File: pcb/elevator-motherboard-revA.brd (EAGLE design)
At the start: 160 x 100 mm, 55 parts, among them J3 MAGJACK, J4 MAGJACK, J5 MAGJACK, J6 POWER_JACK, J8 MAGJACK, Q1 NCV8403BDTRKG, Q2 MOSFET_NCH_DUAL-SO08, Q3 MOSFET_NCH_DUAL-SO08, Q4 MOSFET_NCH_DUAL-SO08, Q5 NCV8403BDTRKG, Q6 MOSFET_NCH_DUAL-SO08, Q7 NCV8403BDTRKG, Q8 NCV8403BDTRKG, Q9 NCV8403BDTRKG, U2 TPD2E001, U3 TPD2E001, U4 74HC2G125, U5 TPD2E001, U7 TPD2E001

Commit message: motherboard schematic is done
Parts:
- removed C19: 0.1uF, microbuilder:0603
- removed PP3, PP4: MC2, con-phoenix-381_l:MC2
- added J1, J10, J7: (no value), SparkFun-Connectors:1X03
- added J9: (no value), SparkFun-Connectors:1X06_NO_SILK
- added LED1, LED2, LED3, LED4: LED-GREEN0603, BeagleBone_Blue_R3:0603-GREEN
- added OUT2: MC4, con-phoenix-381_l:MC4
- added R10, R13, R14, R7, R8, R9: (no value), adafruit:R0603
- added X1, X2, X3, X4: MSTBA2, con-phoenix-508:MSTBA2
- renumbered OUT4 to OUT1
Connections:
- new net B2B_RX1: J9.5, U$1.0/RX
- new net B2B_RX2: J9.6, U$1.2
- new net B2B_TX1: J9.3, U$1.1/TX
- new net B2B_TX2: J9.4, U$1.3/CANTX
- new net BOARD_ID: J10.2, U$1.15/A1
- new net IO1: J2.1, U$1.4/CANRX
- new net IO2: J2.2, U$1.5
- new net IO3: J2.3, U$1.6
- new net IO4: J2.4, U$1.7
- new net IO5: J2.5, U$1.12/MISO
- new net IO6: J2.6, U$1.24
- new net IO7: J2.7, U$1.25
- new net IO8: J2.8, U$1.26
- new net IO9: J2.9, U$1.27
- new net N$23: LED1.A, R9.1
- new net N$24: LED2.A, R10.1
- new net N$25: LED3.A, R7.1
- new net N$26: LED4.A, R8.1
- new net N$27: J10.3, R13.1
- new net N$33: J10.1, R14.2
- new net N$50: U$1.23/A9
- new net N$51: U$1.22/A8
- new net N$60: U$1.13/SCK
- new net N$61: U$1.GND2
- net 12V: now also J1.1, J2.10, J7.1, J7.2, OUT1.1, R8.2, X3.1; no longer OUT1.4
- net 24V: now also J1.2, J1.3, J7.3, OUT1.4, OUT2.4, R10.2, X1.1, X2.1; no longer PP3.1, PP4.1
- net 5V: now also OUT2.1, R7.2, U$1.VIN, X4.1; no longer OUT1.1
- net A.M1: now also U$1.30
- net A.M2: now also U$1.31/A12
- net A.SW1: now also U$1.28
- net A.SW2: now also U$1.29
- net B.M1: now also U$1.34/A15
- net B.M2: now also U$1.33/A14
- net B.SW1: now also U$1.32/A13
- net B.SW2: now also U$1.35/A16
- net C.M1: now also U$1.37/A18
- net C.M2: now also U$1.36/A17
- net C.SW1: now also U$1.39/A20
- net C.SW2: now also U$1.38/A19
- net D.M1: now also U$1.19/A5/SCL
- net D.M2: now also U$1.18/A4/SDA
- net D.SW1: now also U$1.9/CS
- net D.SW2: now also U$1.11/MOSI
- net GND: now also J2.12, J9.2, LED1.C, LED2.C, LED3.C, LED4.C, OUT2.2, OUT2.3, R14.1, X1.2, X2.2, X3.2, X4.2; no longer PP3.2, PP4.2
- net LEDS1: now also U$1.8
- net LEDS2: now also U$1.10/CS
- net PWM1: now also U$1.14/A0
- net PWM2: now also U$1.16/A2
- net PWM3: now also U$1.17/A3
- net PWM4: now also U$1.20/A6
- net PWM5: now also U$1.21/A7
- net VCC: now also J2.11, J9.1, R13.2, R9.2

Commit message: backup
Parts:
- moved X3 191.7 mm to (146.0, 88.0), turned to 90 degrees
- moved J7 174.8 mm to (130.0, 91.0), turned to 90 degrees
- moved R13 170.2 mm to (9.00, 82.0)
- moved R14 168.2 mm to (9.00, 76.0)
- moved J10 160.0 mm to (4.00, 77.0), turned to 90 degrees
- moved J1 159.1 mm to (112.0, 91.0), turned to 90 degrees
- moved X4 157.1 mm to (10.0, 98.0), turned to 180 degrees
- moved LED1 153.9 mm to (88.0, 59.0)
- moved LED2 153.9 mm to (91.0, 59.0)
- moved LED3 153.9 mm to (94.0, 59.0)
- moved LED4 153.9 mm to (88.0, 53.0)
- moved R10 153.9 mm to (92.0, 54.0)
- moved R7 153.9 mm to (88.0, 48.0)
- moved R8 153.9 mm to (91.0, 48.0)
- moved R9 153.9 mm to (94.0, 48.0)
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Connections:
- new net N$34: J7.2, PP1.1
- net 12V: no longer J7.2, PP1.1
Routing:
- net 24V: track 0.00 -> 241.0 mm
- net PWM1: track 0.00 -> 92.8 mm
- net PWM2: track 0.00 -> 84.8 mm
- net PWM3: track 0.00 -> 79.3 mm
- net PWM4: track 0.00 -> 77.5 mm
- net PWM5: track 0.00 -> 70.0 mm
- net 12V: track 0.00 -> 62.8 mm
- added copper zone on layer 1, net GND
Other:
- board size 160 x 100 mm -> 148 x 100 mm

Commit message: wip
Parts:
- moved C10 8.68 mm to (55.9, 88.2), turned to 180 degrees
- moved C1 7.54 mm to (72.5, 88.3), turned to 180 degrees
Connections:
- new net N$35: J1.2, PP2.1
- net 24V: no longer J1.2, PP2.1
- net GND: now also Q5.3, Q7.3, Q8.3, Q9.3
- net N$5: now also PL2.2; no longer PL1.2
- net N$6: now also PL1.2; no longer PL2.2
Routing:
- net 5V: track 0.00 -> 90.9 mm
- net LEDS1: track 0.00 -> 49.7 mm, vias 0 -> 1
- net LEDS2: track 0.00 -> 47.3 mm, vias 0 -> 1
- net N$5: track 0.00 -> 18.2 mm
- net N$6: track 0.00 -> 17.6 mm
- net N$16: track 0.00 -> 17.2 mm
- net N$13: track 0.00 -> 15.8 mm
- net N$15: track 0.00 -> 15.1 mm
- net N$14: track 0.00 -> 13.7 mm
- net N$4: track 0.00 -> 13.3 mm
- net N$35: track 0.00 -> 6.84 mm
- net N$34: track 0.00 -> 6.65 mm
- net 12V: track 62.8 -> 60.2 mm

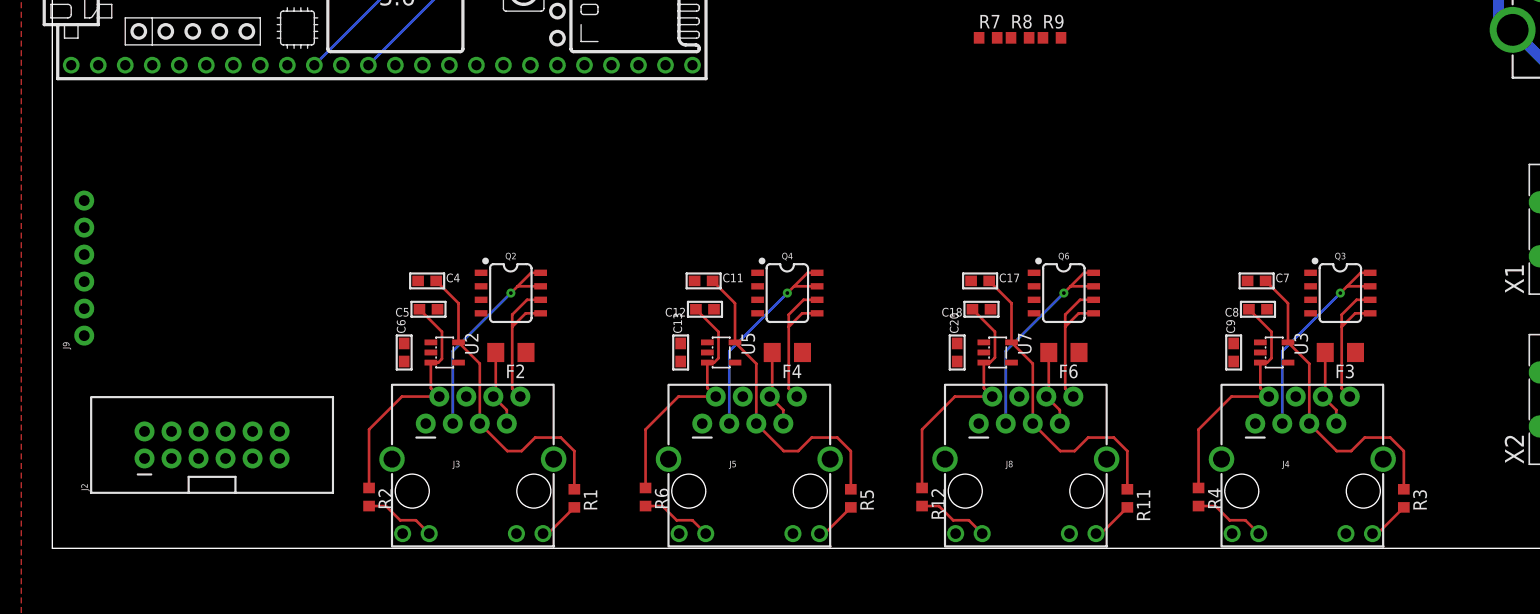
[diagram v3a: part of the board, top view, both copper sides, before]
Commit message: better placement
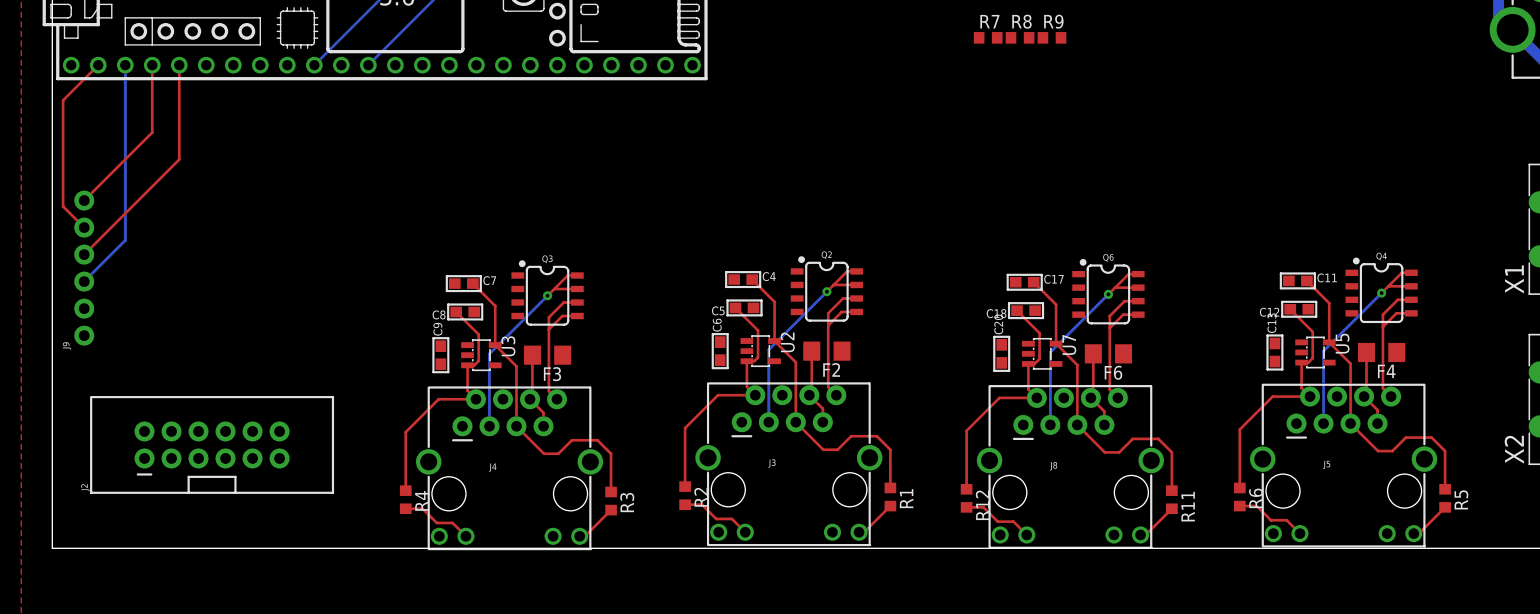
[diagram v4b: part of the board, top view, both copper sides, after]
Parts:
- moved C7 74.5 mm to (38.7, 24.9)
- moved R3 74.5 mm to (52.5, 4.45)
- moved R4 74.5 mm to (33.2, 4.57)
- moved U3 74.5 mm to (40.3, 18.2)
- moved C8 74.5 mm to (38.8, 22.2)
- moved C9 74.5 mm to (36.5, 18.2)
- moved F3 74.5 mm to (46.6, 18.2)
- moved J4 74.5 mm to (35.4, -5.97)
- moved Q3 74.5 mm to (46.6, 23.7)
- moved F4 55.9 mm to (125.0, 18.4)
- moved Q4 55.9 mm to (125.0, 24.0)
- moved R5 55.9 mm to (131.0, 4.70)
- moved C12 55.9 mm to (117.3, 22.5)
- moved C13 55.9 mm to (115.0, 18.4)
- moved J5 55.9 mm to (113.8, -5.71)
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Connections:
- net B.SW1: now also U$1.36/A17; no longer U$1.32/A13
- net C.M1: now also U$1.38/A19; no longer U$1.37/A18
- net C.M2: now also U$1.37/A18; no longer U$1.36/A17
- net C.SW1: now also U$1.32/A13; no longer U$1.39/A20
- net C.SW2: now also U$1.39/A20; no longer U$1.38/A19
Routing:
- net B2B_TX1: track 0.00 -> 22.0 mm
- net B2B_TX2: track 0.00 -> 21.5 mm
- net B2B_RX1: track 0.00 -> 17.5 mm
- net B2B_RX2: track 0.00 -> 15.4 mm

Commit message: wip
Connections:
- removed net N$61: U$1.GND2
- net GND: now also U$1.GND, U$1.GND2
- net IO1: now also U$1.6; no longer U$1.4/CANRX
- net IO2: now also U$1.7; no longer U$1.5
- net IO3: now also U$1.5; no longer U$1.6
- net IO4: now also U$1.12/MISO; no longer U$1.7
- net IO5: now also U$1.4/CANRX; no longer U$1.12/MISO
- net IO7: now also U$1.27; no longer U$1.25
- net IO8: now also U$1.25; no longer U$1.26
- net IO9: now also U$1.26; no longer U$1.27
- net VCC: now also U$1.3V3
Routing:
- net 5V: track 90.9 -> 338.3 mm, vias 0 -> 4
- net B.M1: track 0.00 -> 82.7 mm
- net B.SW1: track 23.6 -> 105.7 mm
- net B.M2: track 0.00 -> 79.2 mm
- net B.SW2: track 29.7 -> 108.3 mm
- net C.M1: track 0.00 -> 67.4 mm
- net IO7: track 0.00 -> 65.6 mm
- net C.SW2: track 29.7 -> 93.2 mm
- net C.M2: track 0.00 -> 62.7 mm
- net IO9: track 0.00 -> 56.5 mm
- net D.M1: track 0.00 -> 54.4 mm, vias 0 -> 1
- net IO5: track 0.00 -> 53.3 mm
- net D.M2: track 0.00 -> 49.8 mm, vias 0 -> 1
- net IO3: track 0.00 -> 49.3 mm
- net IO8: track 0.00 -> 45.3 mm
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- added copper zone on layer 16, net VCC

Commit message: Done with routing
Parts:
- added C2: 0.1uF, microbuilder:0603
- added H1, H2, H3, H4: MOUNT-HOLE3.2, holes:3,2
- moved LED2 14.3 mm to (102.7, 50.7), turned to 180 degrees
- moved LED1 12.6 mm to (97.5, 50.7), turned to 180 degrees
- moved R10 10.8 mm to (102.6, 56.1), turned to 90 degrees
- moved LED3 10.6 mm to (87.4, 50.7), turned to 180 degrees
- moved R9 8.89 mm to (97.5, 56.2), turned to 90 degrees
- moved R8 8.21 mm to (92.5, 56.1), turned to 90 degrees
- moved R7 8.15 mm to (87.4, 56.1), turned to 90 degrees
- moved X4 5.08 mm to (15.1, 98.0)
- moved LED4 5.06 mm to (92.5, 50.6), turned to 180 degrees
- moved J2 4.02 mm to (18.8, 11.0)
- moved OUT1 3.81 mm to (142.8, 66.3)
- moved X3 3.81 mm to (146.0, 84.2)
- moved OUT2 3.81 mm to (31.8, 94.9)
- moved PL1 1.27 mm to (50.6, 94.9)
- moved X1 1.27 mm to (146.0, 31.3)
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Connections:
- net 5V: now also C2.2
- net GND: now also C2.1
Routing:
- net 12V: track 60.2 -> 224.8 mm, vias 0 -> 1
- net BOARD_ID: track 0.00 -> 36.1 mm
- net 24V: track 241.0 -> 273.2 mm
- net VCC: track 0.00 -> 24.0 mm, vias 0 -> 6
- net 5V: track 338.3 -> 348.1 mm, vias 4 -> 5
- net N$27: track 0.00 -> 4.18 mm
- net N$33: track 0.00 -> 4.10 mm
- net N$26: track 0.00 -> 3.72 mm
- net N$23: track 0.00 -> 3.70 mm
- net N$25: track 0.00 -> 3.68 mm
- net N$24: track 0.00 -> 3.64 mm
- net IO9: track 56.5 -> 53.7 mm
- net IO8: track 45.3 -> 42.4 mm
- net IO7: track 65.6 -> 62.8 mm
- net IO6: track 45.3 -> 42.4 mm
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
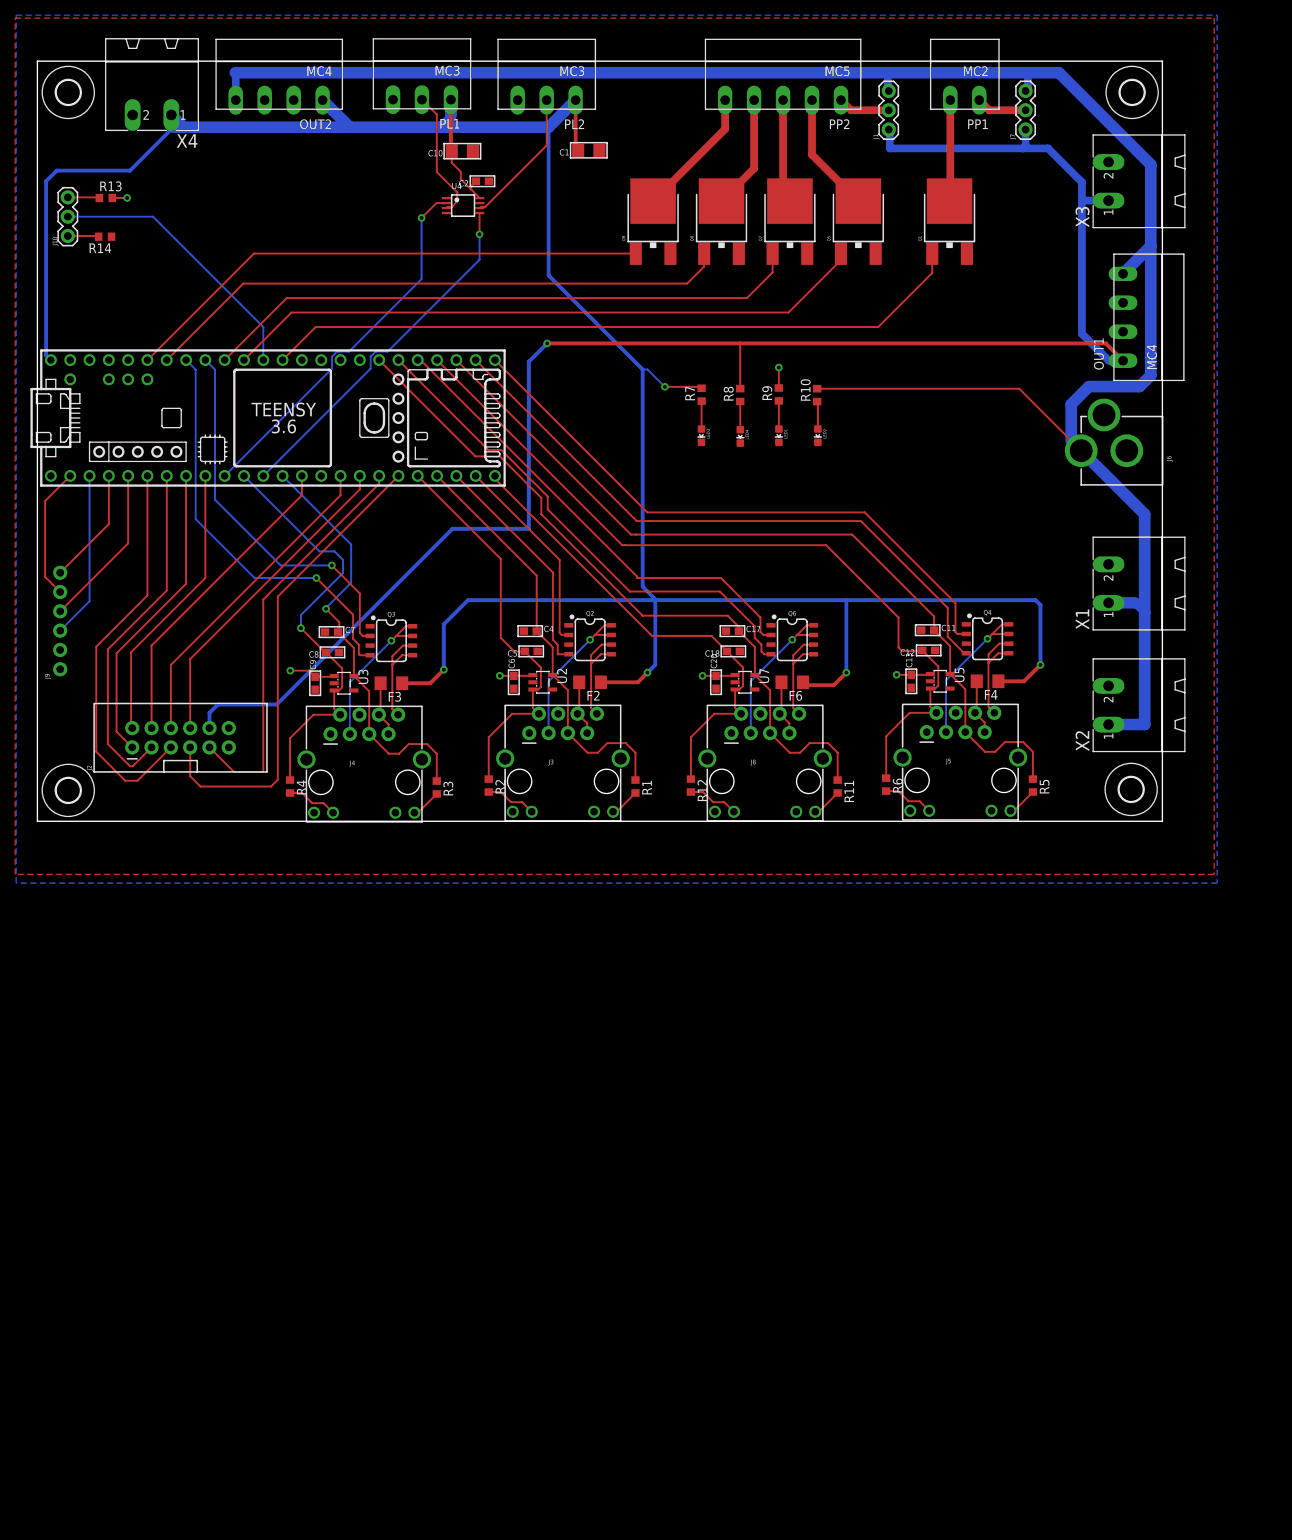
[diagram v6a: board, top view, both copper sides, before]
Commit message: Added silkscreen
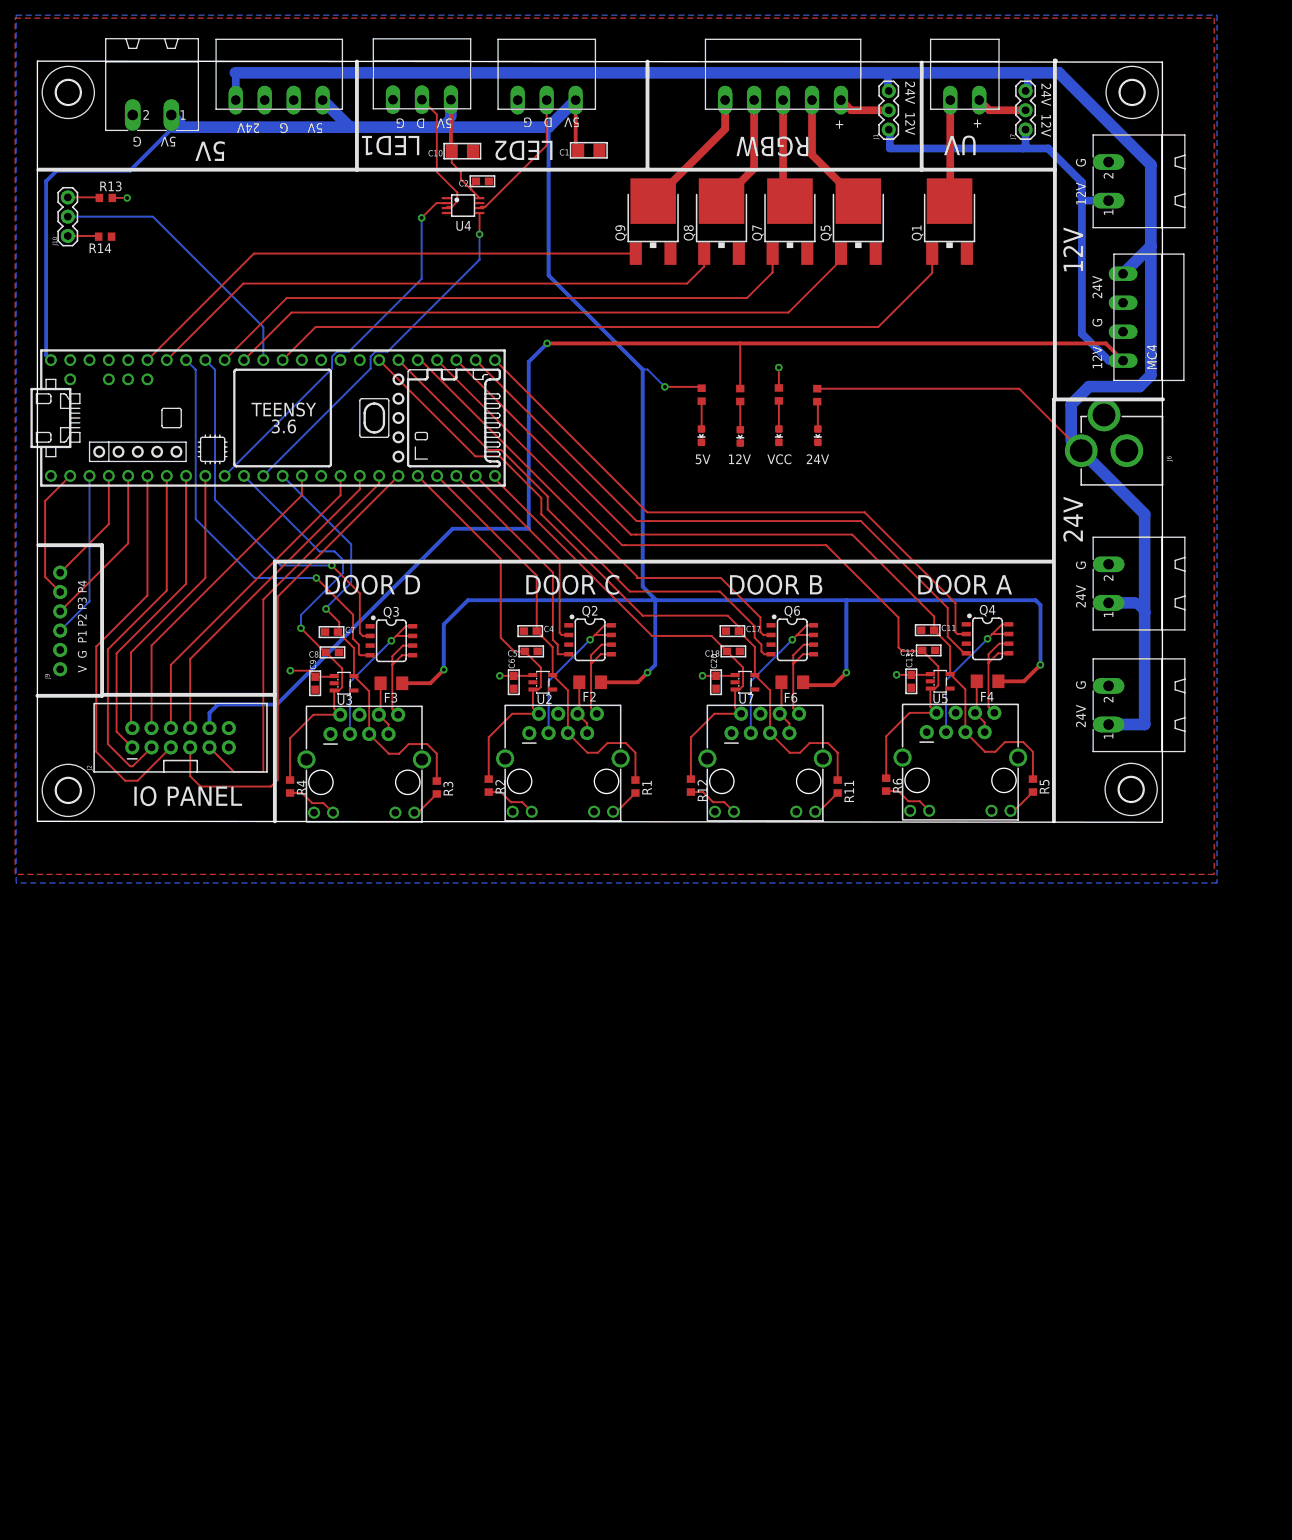
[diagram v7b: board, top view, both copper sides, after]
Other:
- board size 148 x 100 mm -> 148 x 100.1 mm
- board text added: "+"
- board text added: "12V"
- board text added: "12V G"
- board text added: "12V G 24V"
- board text added: "24V"
- board text added: "24V 12V"
- board text added: "24V G"
- board text added: "5V"
- board text added: "5V D G"
- board text added: "5V G"
- board text added: "5V G 24V"
- board text added: "DOOR A"
- board text added: "DOOR B"
- board text added: "DOOR C"
- board text added: "DOOR D"
- board text added: "IO PANEL"
- board text added: "LED1"
- board text added: "LED2"
- board text added: "RGBW"
- board text added: "UV"
- board text added: "V G P1 P2 P3 P4"
- board text added: "VCC"
